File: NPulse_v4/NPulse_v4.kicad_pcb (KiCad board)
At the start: 4 copper layers, 39.8 x 70 mm, 162 parts, among them IC1 TXU0202QDCUR, IC2 DRV8220DSGR, IC3 DRV8220DSGR, IC4 DRV8220DSGR, IC5 DRV8220DSGR, IC6 DRV8220DSGR, IC7 DRV8220DSGR, IC8 DRV8220DSGR, IC9 DRV8220DSGR, J10 Conn_02x05_Odd_Even, J2 Conn_01x04_Pin, J3 Conn_01x06_Pin, J4 Conn_01x04_Pin, J5 Conn_02x05_Odd_Even, J6 Conn_02x05_Odd_Even, J7 Conn_02x05_Odd_Even, J8 Conn_02x05_Odd_Even, J9 Conn_02x05_Odd_Even, Q1 PMOS, Q2 NMOS, SW1 SW_Push, SW2 SW_SPDT, U1 STM32G484METx, U10 TPS7A0533PDBZ, U2 SN74LVC002, U3 SN74LVC002, U4 SN74LVC002, U5 SN74LVC002, U6 SN74LVC002, U7 SN74LVC002, U8 SN74LVC002, U9 SN74LVC002, Y1 16MHz

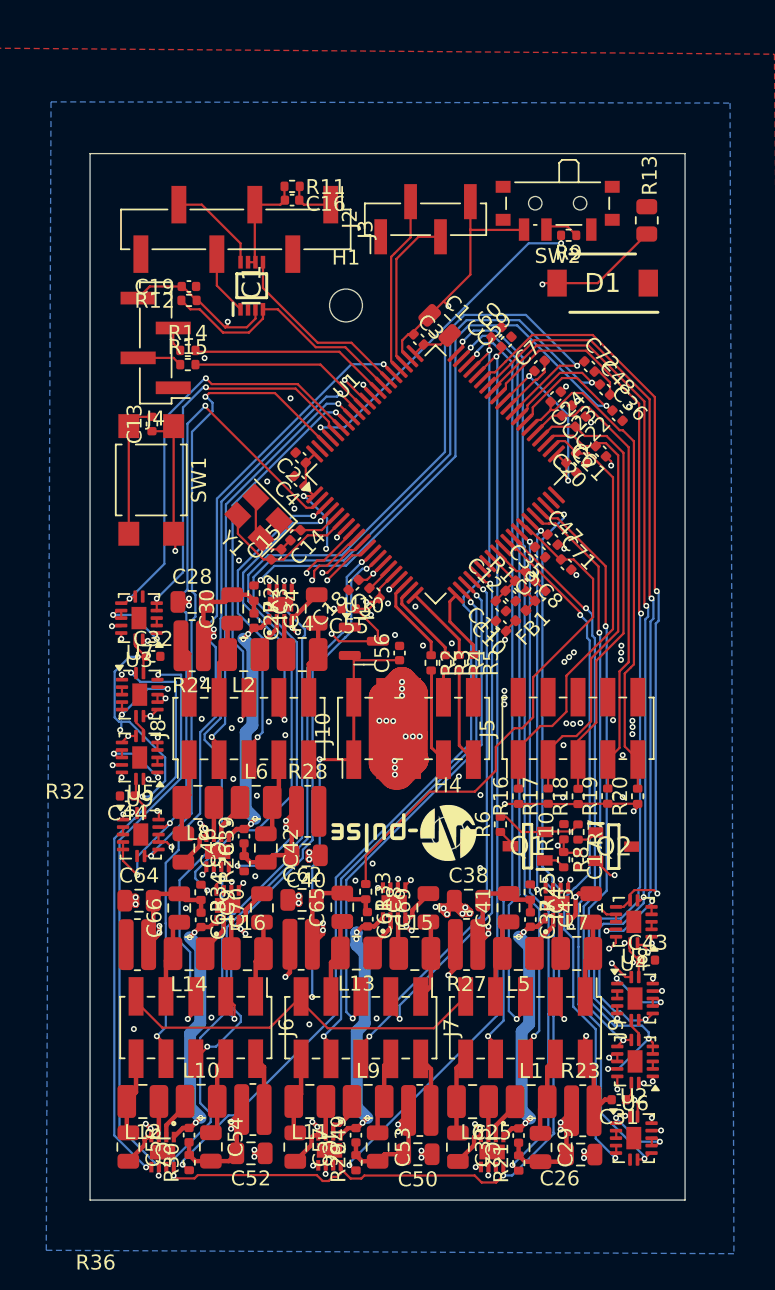
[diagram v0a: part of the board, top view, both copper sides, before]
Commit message: Udate mounting holes positions
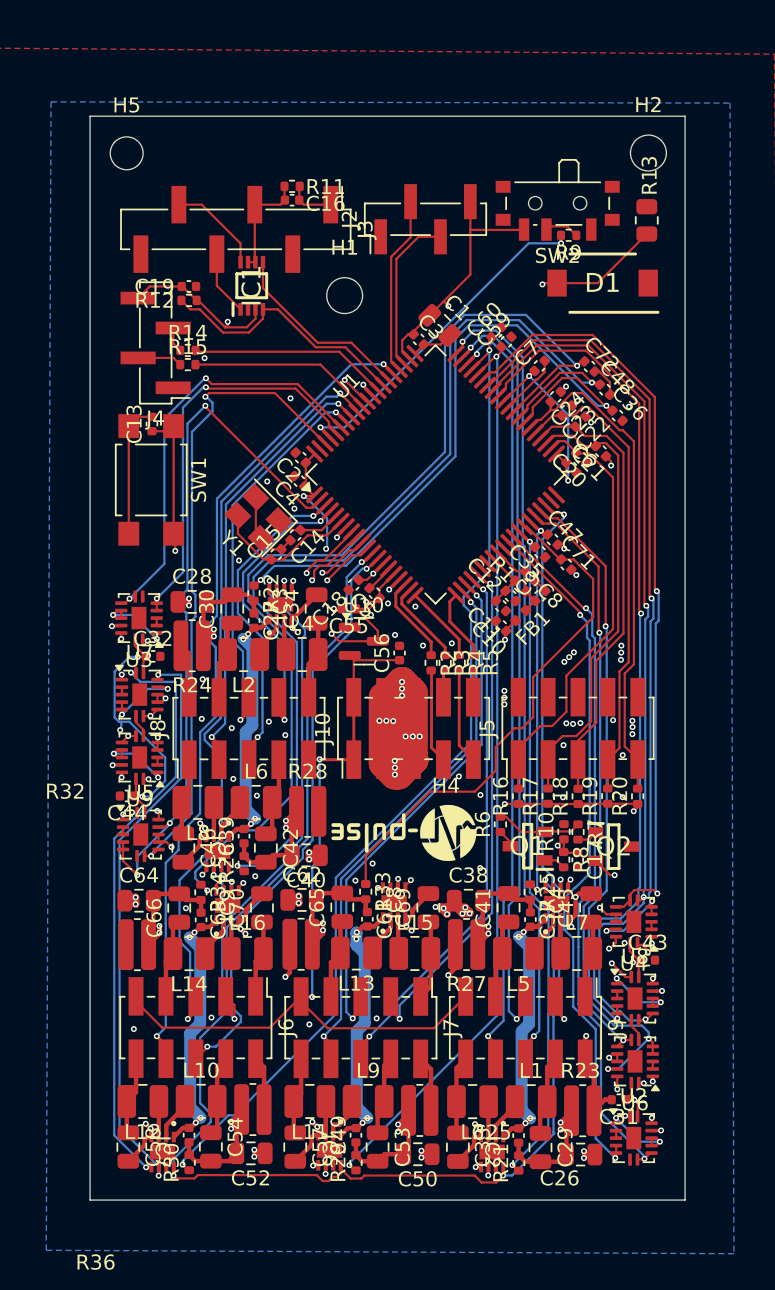
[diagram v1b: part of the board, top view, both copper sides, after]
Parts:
- added H2: MountingHole, MountingHole:MountingHole_2.2mm_M2, F.Cu at (190.7, 67.6)
- added H5: MountingHole, MountingHole:MountingHole_2.2mm_M2, F.Cu at (155.8, 67.6)
- moved H1 0.67 mm to (170.4, 77.2)
- moved H4 0.11 mm to (177.2, 113.2)
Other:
- board size 39.8 x 70 mm -> 39.8 x 72.5 mm
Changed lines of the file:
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@@
 		)
 	)
-	(footprint "MountingHole:MountingHole_2.2mm_M2"
-		(layer "F.Cu")
-		(at 177.28 113.12)
-		(descr "Mounting Hole 2.2mm, no annular, M2")
-		(tags "mounting hole 2.2mm no annular m2")
-		(property "Reference" "H4"
-			(at 0 -3.2 0)
-			(layer "F.SilkS")
-			(effects
-				(font
-					(size 1 1)
-					(thickness 0.15)
-				)
-			)
-		)
-		(property "Value" "MountingHole"
-			(at 0 3.2 0)
-			(layer "F.Fab")
-			(effects
-				(font
-					(size 1 1)
-					(thickness 0.15)
-				)
-			)
-		)
-		(property "Datasheet" ""
-			(at 0 0 0)
-			(unlocked yes)
-			(layer "F.Fab")
-			(hide yes)
-			(effects
-				(font
-					(size 1.27 1.27)
-					(thickness 0.15)
-				)
-			)
-		)
-		(property "Description" "Mounting Hole without connection"
-			(at 0 0 0)
-			(unlocked yes)
-			(layer "F.Fab")
-			(hide yes)
-			(effects
-				(font
-					(size 1.27 1.27)
-					(thickness 0.15)
-				)
-			)
-		)
-		(property ki_fp_filters "MountingHole*")
-		(sheetname "/")
-		(sheetfile "NPulse_v4.kicad_sch")
-		(attr exclude_from_pos_files exclude_from_bom)
-		(fp_circle
-			(center 0 0)
-			(end 2.2 0)
-			(stroke
-				(width 0.15)
-				(type solid)
-			)
-			(fill no)
-			(layer "Cmts.User")
-		)
-		(fp_circle
-			(center 0 0)
-			(end 2.45 0)
-			(stroke
-				(width 0.05)
-				(type solid)
-			)
-			(fill no)
-			(layer "F.CrtYd")
-		)
-		(fp_text user "${REFERENCE}"
-			(at 0 0 0)
-			(layer "F.Fab")
-			(effects
-				(font
-					(size 1 1)
-					(thickness 0.15)
-				)
-			)
-		)
-		(pad "" np_thru_hole circle
-			(at 0 0)
-			(size 2.2 2.2)
-			(drill 2.2)
-			(layers "*.Cu" "*.Mask")
-		)
-		(embedded_fonts no)
-	)
 	(footprint "Capacitor_SMD:C_0402_1005Metric"
 		(layer "F.Cu")
@@
 		(model "${KICAD8_3DMODEL_DIR}/Button_Switch_SMD.3dshapes/SW_SPDT_PCM12.wrl"
 			(offset
-				(xyz 0 0 0)
+				(xyz 0 0 1)
 			)
 			(scale
@@
 			)
 			(rotate
-				(xyz 0 0 0)
+				(xyz -0 -0 -0)
 			)
 		)
@@
 		)
 	)
+	(footprint "MountingHole:MountingHole_2.2mm_M2"
+		(layer "F.Cu")
+		(at 190.71 67.62)
+		(descr "Mounting Hole 2.2mm, no annular, M2")
+		(tags "mounting hole 2.2mm no annular m2")
+		(property "Reference" "H2"
+			(at 0 -3.2 0)
+			(layer "F.SilkS")
+			(effects
+				(font
+					(size 1 1)
+					(thickness 0.15)
+				)
+			)
+		)
+		(property "Value" "MountingHole"
+			(at 0 3.2 0)
+			(layer "F.Fab")
+			(effects
+				(font
+					(size 1 1)
+					(thickness 0.15)
+				)
+			)
+		)
+		(property "Datasheet" ""
+			(at 0 0 0)
+			(unlocked yes)
+			(layer "F.Fab")
+			(hide yes)
+			(effects
+				(font
+					(size 1.27 1.27)
+					(thickness 0.15)
+				)
+			)
+		)
+		(property "Description" "Mounting Hole without connection"
+			(at 0 0 0)
+			(unlocked yes)
+			(layer "F.Fab")
+			(hide yes)
+			(effects
+				(font
+					(size 1.27 1.27)
+					(thickness 0.15)
+				)
+			)
+		)
+		(property ki_fp_filters "MountingHole*")
+		(sheetname "/")
+		(sheetfile "NPulse_v4.kicad_sch")
+		(attr exclude_from_pos_files exclude_from_bom)
+		(fp_circle
+			(center 0 0)
+			(end 2.2 0)
+			(stroke
+				(width 0.15)
+				(type solid)
+			)
+			(fill no)
+			(layer "Cmts.User")
+		)
+		(fp_circle
+			(center 0 0)
+			(end 2.45 0)
+			(stroke
+				(width 0.05)
+				(type solid)
+			)
+			(fill no)
+			(layer "F.CrtYd")
+		)
+		(fp_text user "${REFERENCE}"
+			(at 0 0 0)
+			(layer "F.Fab")
+			(effects
+				(font
+					(size 1 1)
+					(thickness 0.15)
+				)
+			)
+		)
+		(pad "" np_thru_hole circle
+			(at 0 0)
+			(size 2.4 2.4)
+			(drill 2.4)
+			(layers "F&B.Cu" "*.Mask")
+		)
+		(embedded_fonts no)
+	)
 	(footprint "Capacitor_SMD:C_0402_1005Metric"
 		(layer "F.Cu")
@@
 		)
 	)
+	(footprint "MountingHole:MountingHole_2.2mm_M2"
+		(layer "F.Cu")
+		(at 177.17 113.15)
+		(descr "Mounting Hole 2.2mm, no annular, M2")
+		(tags "mounting hole 2.2mm no annular m2")
+		(property "Reference" "H4"
+			(at 0 -3.2 0)
+			(layer "F.SilkS")
+			(effects
+				(font
+					(size 1 1)
+					(thickness 0.15)
+				)
+			)
+		)
+		(property "Value" "MountingHole"
+			(at 0 3.2 0)
+			(layer "F.Fab")
+			(effects
+				(font
+					(size 1 1)
+					(thickness 0.15)
+				)
+			)
+		)
+		(property "Datasheet" ""
+			(at 0 0 0)
+			(unlocked yes)
+			(layer "F.Fab")
+			(hide yes)
+			(effects
+				(font
+					(size 1.27 1.27)
+					(thickness 0.15)
+				)
+			)
+		)
+		(property "Description" "Mounting Hole without connection"
+			(at 0 0 0)
+			(unlocked yes)
+			(layer "F.Fab")
+			(hide yes)
+			(effects
+				(font
+					(size 1.27 1.27)
+					(thickness 0.15)
+				)
+			)
+		)
+		(property ki_fp_filters "MountingHole*")
+		(sheetname "/")
+		(sheetfile "NPulse_v4.kicad_sch")
+		(attr exclude_from_pos_files exclude_from_bom)
+		(fp_circle
+			(center 0 0)
+			(end 2.2 0)
+			(stroke
+				(width 0.15)
+				(type solid)
+			)
+			(fill no)
+			(layer "Cmts.User")
+		)
+		(fp_circle
+			(center 0 0)
+			(end 2.45 0)
+			(stroke
+				(width 0.05)
+				(type solid)
+			)
+			(fill no)
+			(layer "F.CrtYd")
+		)
+		(fp_text user "${REFERENCE}"
+			(at 0 0 0)
+			(layer "F.Fab")
+			(effects
+				(font
+					(size 1 1)
+					(thickness 0.15)
+				)
+			)
+		)
+		(pad "" np_thru_hole circle
+			(at 0 0)
+			(size 2.4 2.4)
+			(drill 2.4)
+			(layers "F&B.Cu" "*.Mask")
+		)
+		(embedded_fonts no)
+	)
 	(footprint "Capacitor_SMD:C_0805_2012Metric"
 		(layer "F.Cu")
@@
 	(footprint "MountingHole:MountingHole_2.2mm_M2"
 		(layer "F.Cu")
-		(at 170.48 77.82)
+		(at 155.81 67.64)
 		(descr "Mounting Hole 2.2mm, no annular, M2")
 		(tags "mounting hole 2.2mm no annular m2")
-		(property "Reference" "H1"
+		(property "Reference" "H5"
 			(at 0 -3.2 0)
 			(layer "F.SilkS")
@@
 		(embedded_fonts no)
 	)
+	(footprint "MountingHole:MountingHole_2.2mm_M2"
+		(layer "F.Cu")
+		(at 170.39 77.16)
+		(descr "Mounting Hole 2.2mm, no annular, M2")
+		(tags "mounting hole 2.2mm no annular m2")
+		(property "Reference" "H1"
+			(at 0 -3.2 0)
+			(layer "F.SilkS")
+			(effects
+				(font
+					(size 1 1)
+					(thickness 0.15)
+				)
+			)
+		)
+		(property "Value" "MountingHole"
+			(at 0 3.2 0)
+			(layer "F.Fab")
+			(effects
+				(font
+					(size 1 1)
+					(thickness 0.15)
+				)
+			)
+		)
+		(property "Datasheet" ""
+			(at 0 0 0)
+			(unlocked yes)
+			(layer "F.Fab")
+			(hide yes)
+			(effects
+				(font
+					(size 1.27 1.27)
+					(thickness 0.15)
+				)
+			)
+		)
+		(property "Description" "Mounting Hole without connection"
+			(at 0 0 0)
+			(unlocked yes)
+			(layer "F.Fab")
+			(hide yes)
+			(effects
+				(font
+					(size 1.27 1.27)
+					(thickness 0.15)
+				)
+			)
+		)
+		(property ki_fp_filters "MountingHole*")
+		(sheetname "/")
+		(sheetfile "NPulse_v4.kicad_sch")
+		(attr exclude_from_pos_files exclude_from_bom)
+		(fp_circle
+			(center 0 0)
+			(end 2.2 0)
+			(stroke
+				(width 0.15)
+				(type solid)
+			)
+			(fill no)
+			(layer "Cmts.User")
+		)
+		(fp_circle
+			(center 0 0)
+			(end 2.45 0)
+			(stroke
+				(width 0.05)
+				(type solid)
+			)
+			(fill no)
+			(layer "F.CrtYd")
+		)
+		(fp_text user "${REFERENCE}"
+			(at 0 0 0)
+			(layer "F.Fab")
+			(effects
+				(font
+					(size 1 1)
+					(thickness 0.15)
+				)
+			)
+		)
+		(pad "" np_thru_hole circle
+			(at 0 0)
+			(size 2.4 2.4)
+			(drill 2.4)
+			(layers "F&B.Cu" "*.Mask")
+		)
+		(embedded_fonts no)
+	)
 	(footprint "Inductor_SMD:L_1008_2520Metric"
 		(layer "F.Cu")
@@
 	)
 	(gr_rect
-		(start 154.96 69.25)
+		(start 154.96 66.75)
 		(end 191.56 136.05)
 		(stroke
 			(width 0.1)
-			(type default)
+			(type solid)
 		)
 		(fill no)
@@
 	)
 	(gr_rect
-		(start 153.36 67.66)
+		(start 153.36 65.16)
 		(end 193.16 137.66)
 		(stroke
 			(width 0.05)
-			(type default)
+			(type solid)
 		)
 		(fill no)

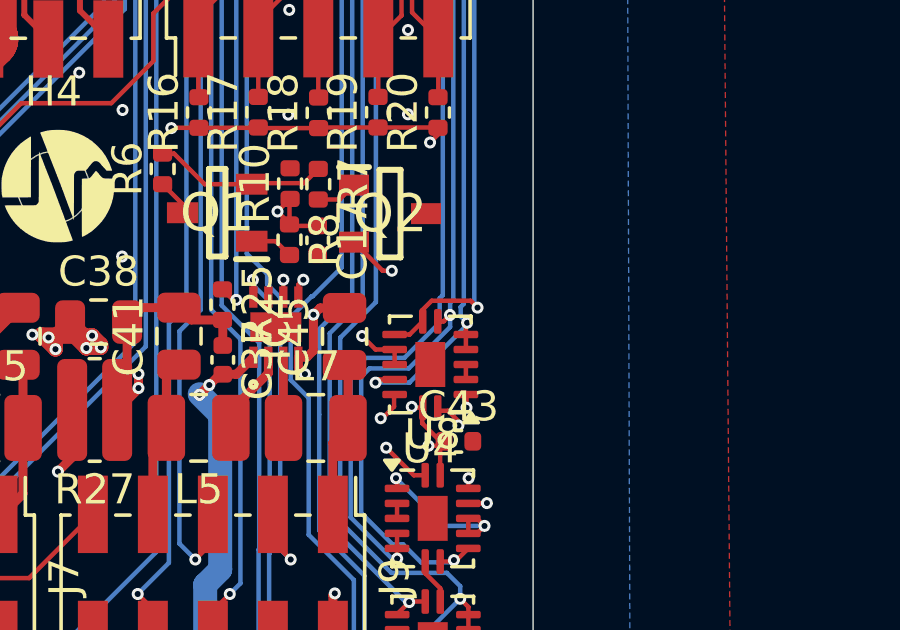
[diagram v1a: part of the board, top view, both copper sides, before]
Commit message: remove gnd via from pwm trace and generate gerbers
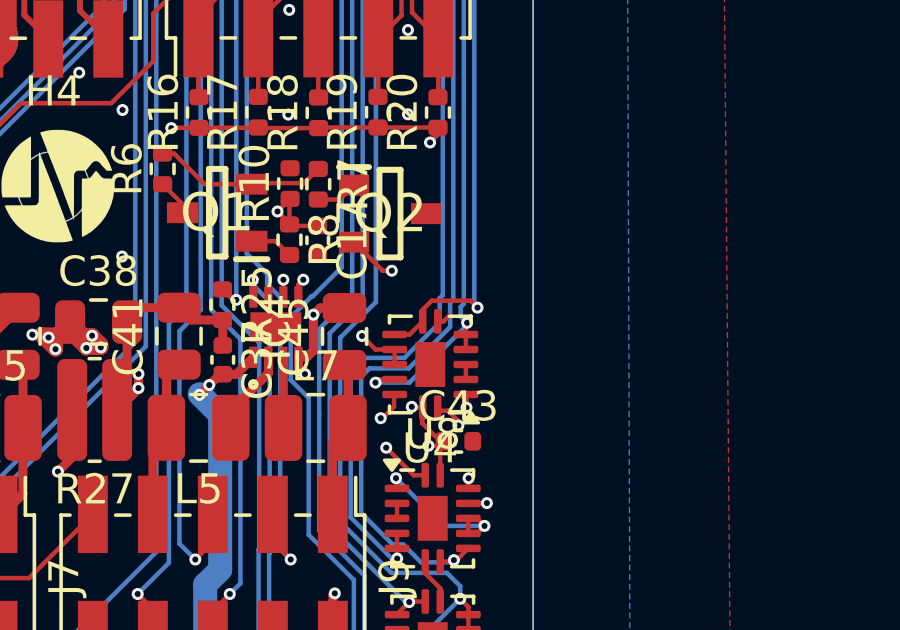
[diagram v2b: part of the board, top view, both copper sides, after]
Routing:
- net GND: vias 61 -> 60
